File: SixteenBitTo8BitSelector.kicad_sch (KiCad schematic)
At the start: 0 parts

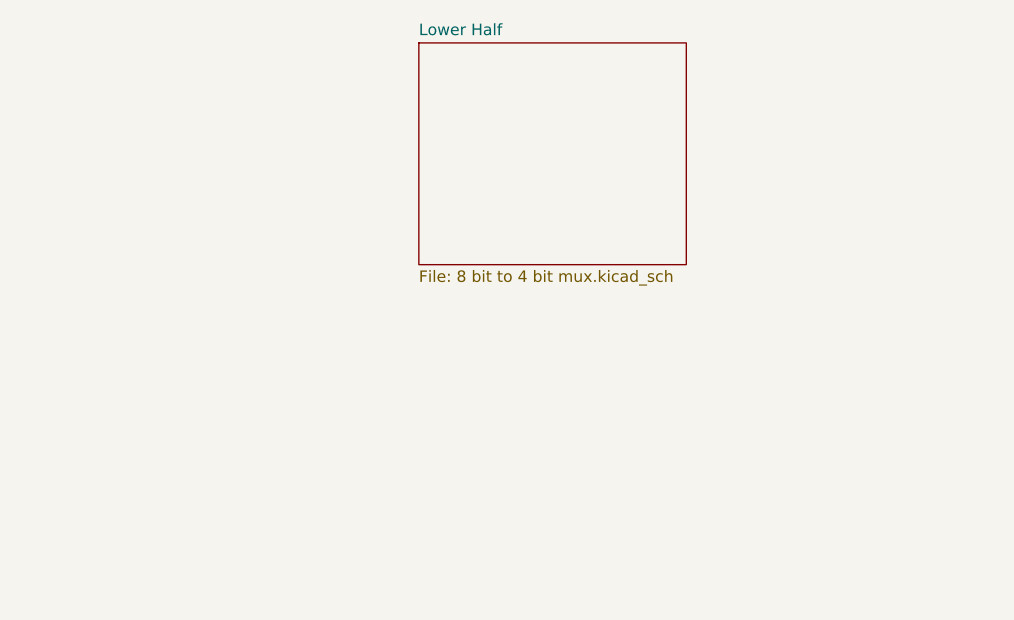
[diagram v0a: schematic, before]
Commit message: Define the muxer in terms of A0-A15
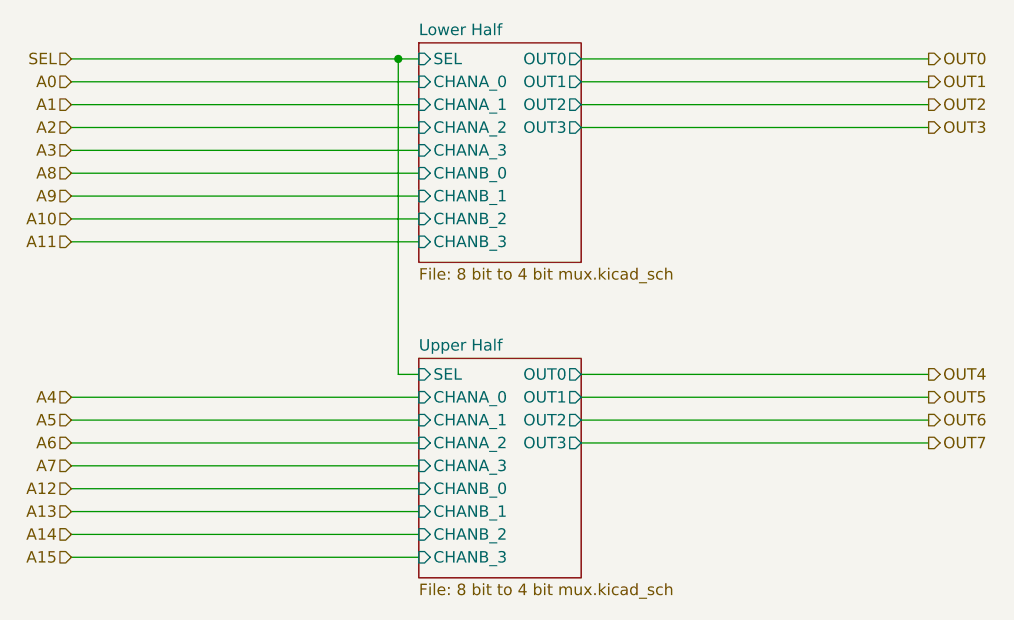
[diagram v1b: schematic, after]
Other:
- added sheet Upper Half (8 bit to 4 bit mux.kicad_sch)
- sheet Lower Half ports: added CHANA_0, CHANA_1, CHANA_2, CHANA_3, CHANB_0, CHANB_1, CHANB_2, CHANB_3, OUT0, OUT1, OUT2, OUT3, SEL; removed none
- company: (none) -> Joshua Scoggins
- title: (none) -> 16 Bit value to 8 bit muxer
